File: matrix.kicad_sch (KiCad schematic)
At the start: 0 parts

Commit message: Placing Finished
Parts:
- added D1, D10, D11, D12, D13, D14, D15, D16, D17, D18, D19, D2, D20, D21, D22, D23, D24, D25, D26, D27, D28, D29, D3, D30, D31, D32, D33, D34, D35, D36, D37, D38, D39, D4, D40, D41, D42, D43, D44, D45, D46, D47, D48, D49, D5, D50, D51, D52, D53, D54, D55, D56, D57, D58, D59, D6, D60, D61, D62, D63, D64, D65, D66, D67, D68, D69, D7, D70, D71, D72, D73, D74, D8, D9: SOD-123, Diode_SMD:D_SOD-123, symbol Device:D_Small
- added MX1, MX10, MX11, MX12, MX13, MX14, MX15, MX16, MX17, MX18, MX19, MX2, MX20, MX21, MX22, MX23, MX24, MX25, MX26, MX27, MX28, MX29, MX3, MX30, MX31, MX32, MX33, MX34, MX35, MX36, MX37, MX38, MX39, MX4, MX40, MX41, MX42, MX43, MX44, MX45, MX46, MX47, MX48, MX49, MX5, MX50, MX51, MX52, MX53, MX54, MX55, MX56, MX57, MX58, MX59, MX6, MX60, MX61, MX62, MX63, MX64, MX65, MX66, MX67, MX68, MX69, MX7, MX70, MX71, MX72, MX73, MX74, MX8, MX9: MX-NoLED, marbastlib-mx:SW_MX_HS_1u, symbol MX_Alps_Hybrid:MX-NoLED
- added S73: MX_stab, marbastlib-mx:STAB_MX_2u, symbol marbastlib-mx:MX_stab
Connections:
- new net: D29.2 (A), MX29.2 (ROW)
- new net: D26.2 (A), MX26.2 (ROW)
- new net: D41.2 (A), MX41.2 (ROW)
- new net: D67.2 (A), MX67.2 (ROW)
- new net: D7.2 (A), MX7.2 (ROW)
- new net: D74.2 (A), MX74.2 (ROW)
- new net: D69.2 (A), MX69.2 (ROW)
- new net: D25.2 (A), MX25.2 (ROW)
- new net: D27.2 (A), MX27.2 (ROW)
- new net: D21.2 (A), MX21.2 (ROW)
- new net: D14.2 (A), MX14.2 (ROW)
- new net: D35.2 (A), MX35.2 (ROW)
- new net: D68.2 (A), MX68.2 (ROW)
- new net: D22.2 (A), MX22.2 (ROW)
- new net: D36.2 (A), MX36.2 (ROW)
- new net: D2.2 (A), MX2.2 (ROW)
- new net: D70.2 (A), MX70.2 (ROW)
- new net: D62.2 (A), MX62.2 (ROW)
- new net: D23.2 (A), MX23.2 (ROW)
- new net: D18.2 (A), MX18.2 (ROW)
- new net: D50.2 (A), MX50.2 (ROW)
- new net: D45.2 (A), MX45.2 (ROW)
- new net: D43.2 (A), MX43.2 (ROW)
- new net: D64.2 (A), MX64.2 (ROW)
- new net: D51.2 (A), MX51.2 (ROW)
- new net: D52.2 (A), MX52.2 (ROW)
- new net: D6.2 (A), MX6.2 (ROW)
- new net: D59.2 (A), MX59.2 (ROW)
- new net: D11.2 (A), MX11.2 (ROW)
- new net: D33.2 (A), MX33.2 (ROW)
- new net: D4.2 (A), MX4.2 (ROW)
- new net: D39.2 (A), MX39.2 (ROW)
- new net: D5.2 (A), MX5.2 (ROW)
- new net: D55.2 (A), MX55.2 (ROW)
- new net: D61.2 (A), MX61.2 (ROW)
- new net: D16.2 (A), MX16.2 (ROW)
- new net: D72.2 (A), MX72.2 (ROW)
- new net: D48.2 (A), MX48.2 (ROW)
- new net: D73.2 (A), MX73.2 (ROW)
- new net: D12.2 (A), MX12.2 (ROW)
- new net: D37.2 (A), MX37.2 (ROW)
- new net: D71.2 (A), MX71.2 (ROW)
- new net: D31.2 (A), MX31.2 (ROW)
- new net: D1.2 (A), MX1.2 (ROW)
- new net: D28.2 (A), MX28.2 (ROW)
- new net: D65.2 (A), MX65.2 (ROW)
- new net: D49.2 (A), MX49.2 (ROW)
- new net: D17.2 (A), MX17.2 (ROW)
- new net: D3.2 (A), MX3.2 (ROW)
- new net: D60.2 (A), MX60.2 (ROW)
- new net: D42.2 (A), MX42.2 (ROW)
- new net: D40.2 (A), MX40.2 (ROW)
- new net: D9.2 (A), MX9.2 (ROW)
- new net: D24.2 (A), MX24.2 (ROW)
- new net: D38.2 (A), MX38.2 (ROW)
- new net: D8.2 (A), MX8.2 (ROW)
- new net: D10.2 (A), MX10.2 (ROW)
- new net: D63.2 (A), MX63.2 (ROW)
- new net: D58.2 (A), MX58.2 (ROW)
- new net: D15.2 (A), MX15.2 (ROW)
- new net: D56.2 (A), MX56.2 (ROW)
- new net: D53.2 (A), MX53.2 (ROW)
- new net: D13.2 (A), MX13.2 (ROW)
- new net: D66.2 (A), MX66.2 (ROW)
- new net: D44.2 (A), MX44.2 (ROW)
- new net: D34.2 (A), MX34.2 (ROW)
- new net: D47.2 (A), MX47.2 (ROW)
- new net: D20.2 (A), MX20.2 (ROW)
- new net: D57.2 (A), MX57.2 (ROW)
- new net: D30.2 (A), MX30.2 (ROW)
- new net: D54.2 (A), MX54.2 (ROW)
- new net: D46.2 (A), MX46.2 (ROW)
- new net: D32.2 (A), MX32.2 (ROW)
- new net: D19.2 (A), MX19.2 (ROW)
- new net COL0: MX1.1 (COL), MX10.1 (COL), MX18.1 (COL), MX25.1 (COL), MX33.1 (COL), MX42.1 (COL), MX51.1 (COL), MX57.1 (COL), MX66.1 (COL)
- new net COL2: MX12.1 (COL), MX20.1 (COL), MX27.1 (COL), MX3.1 (COL), MX35.1 (COL), MX44.1 (COL), MX53.1 (COL), MX59.1 (COL), MX68.1 (COL)
- new net COL3: MX13.1 (COL), MX21.1 (COL), MX28.1 (COL), MX36.1 (COL), MX4.1 (COL), MX45.1 (COL), MX54.1 (COL), MX60.1 (COL), MX69.1 (COL)
- new net COL4: MX14.1 (COL), MX22.1 (COL), MX29.1 (COL), MX37.1 (COL), MX46.1 (COL), MX5.1 (COL), MX55.1 (COL), MX61.1 (COL), MX70.1 (COL)
- new net COL5: MX15.1 (COL), MX23.1 (COL), MX30.1 (COL), MX38.1 (COL), MX47.1 (COL), MX56.1 (COL), MX6.1 (COL), MX62.1 (COL), MX71.1 (COL)
- new net COL6: MX16.1 (COL), MX31.1 (COL), MX39.1 (COL), MX48.1 (COL), MX63.1 (COL), MX7.1 (COL), MX72.1 (COL)
- new net COL7: MX17.1 (COL), MX24.1 (COL), MX32.1 (COL), MX40.1 (COL), MX49.1 (COL), MX64.1 (COL), MX73.1 (COL), MX8.1 (COL)
- new net COL8: MX41.1 (COL), MX50.1 (COL), MX65.1 (COL), MX74.1 (COL), MX9.1 (COL)
- new net ROW0: D1.1 (K), D2.1 (K), D3.1 (K), D4.1 (K), D5.1 (K), D6.1 (K), D7.1 (K), D8.1 (K), D9.1 (K)
- new net ROW1: D10.1 (K), D11.1 (K), D12.1 (K), D13.1 (K), D14.1 (K), D15.1 (K), D16.1 (K), D17.1 (K)
- new net ROW2: D18.1 (K), D19.1 (K), D20.1 (K), D21.1 (K), D22.1 (K), D23.1 (K), D24.1 (K)
- new net ROW3: D25.1 (K), D26.1 (K), D27.1 (K), D28.1 (K), D29.1 (K), D30.1 (K), D31.1 (K), D32.1 (K)
- new net ROW4: D33.1 (K), D34.1 (K), D35.1 (K), D36.1 (K), D37.1 (K), D38.1 (K), D39.1 (K), D40.1 (K), D41.1 (K)
- new net ROW5: D42.1 (K), D43.1 (K), D44.1 (K), D45.1 (K), D46.1 (K), D47.1 (K), D48.1 (K), D49.1 (K), D50.1 (K)
- new net ROW6: D51.1 (K), D52.1 (K), D53.1 (K), D54.1 (K), D55.1 (K), D56.1 (K)
- new net ROW7: D57.1 (K), D58.1 (K), D59.1 (K), D60.1 (K), D61.1 (K), D62.1 (K), D63.1 (K), D64.1 (K), D65.1 (K)
- new net ROW8: D66.1 (K), D67.1 (K), D68.1 (K), D69.1 (K), D70.1 (K), D71.1 (K), D72.1 (K), D73.1 (K), D74.1 (K)
- new net cOL1: MX11.1 (COL), MX19.1 (COL), MX2.1 (COL), MX26.1 (COL), MX34.1 (COL), MX43.1 (COL), MX52.1 (COL), MX58.1 (COL), MX67.1 (COL)
- no-connect marks 0 -> 74
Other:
- note added: "Row 0"
- note added: "Row 1"
- note added: "Row 2"
- note added: "Row 3"
- note added: "Row 4"
- note added: "Row 5"
- note added: "Row 6"
- note added: "Row 7"
- note added: "Row 8"

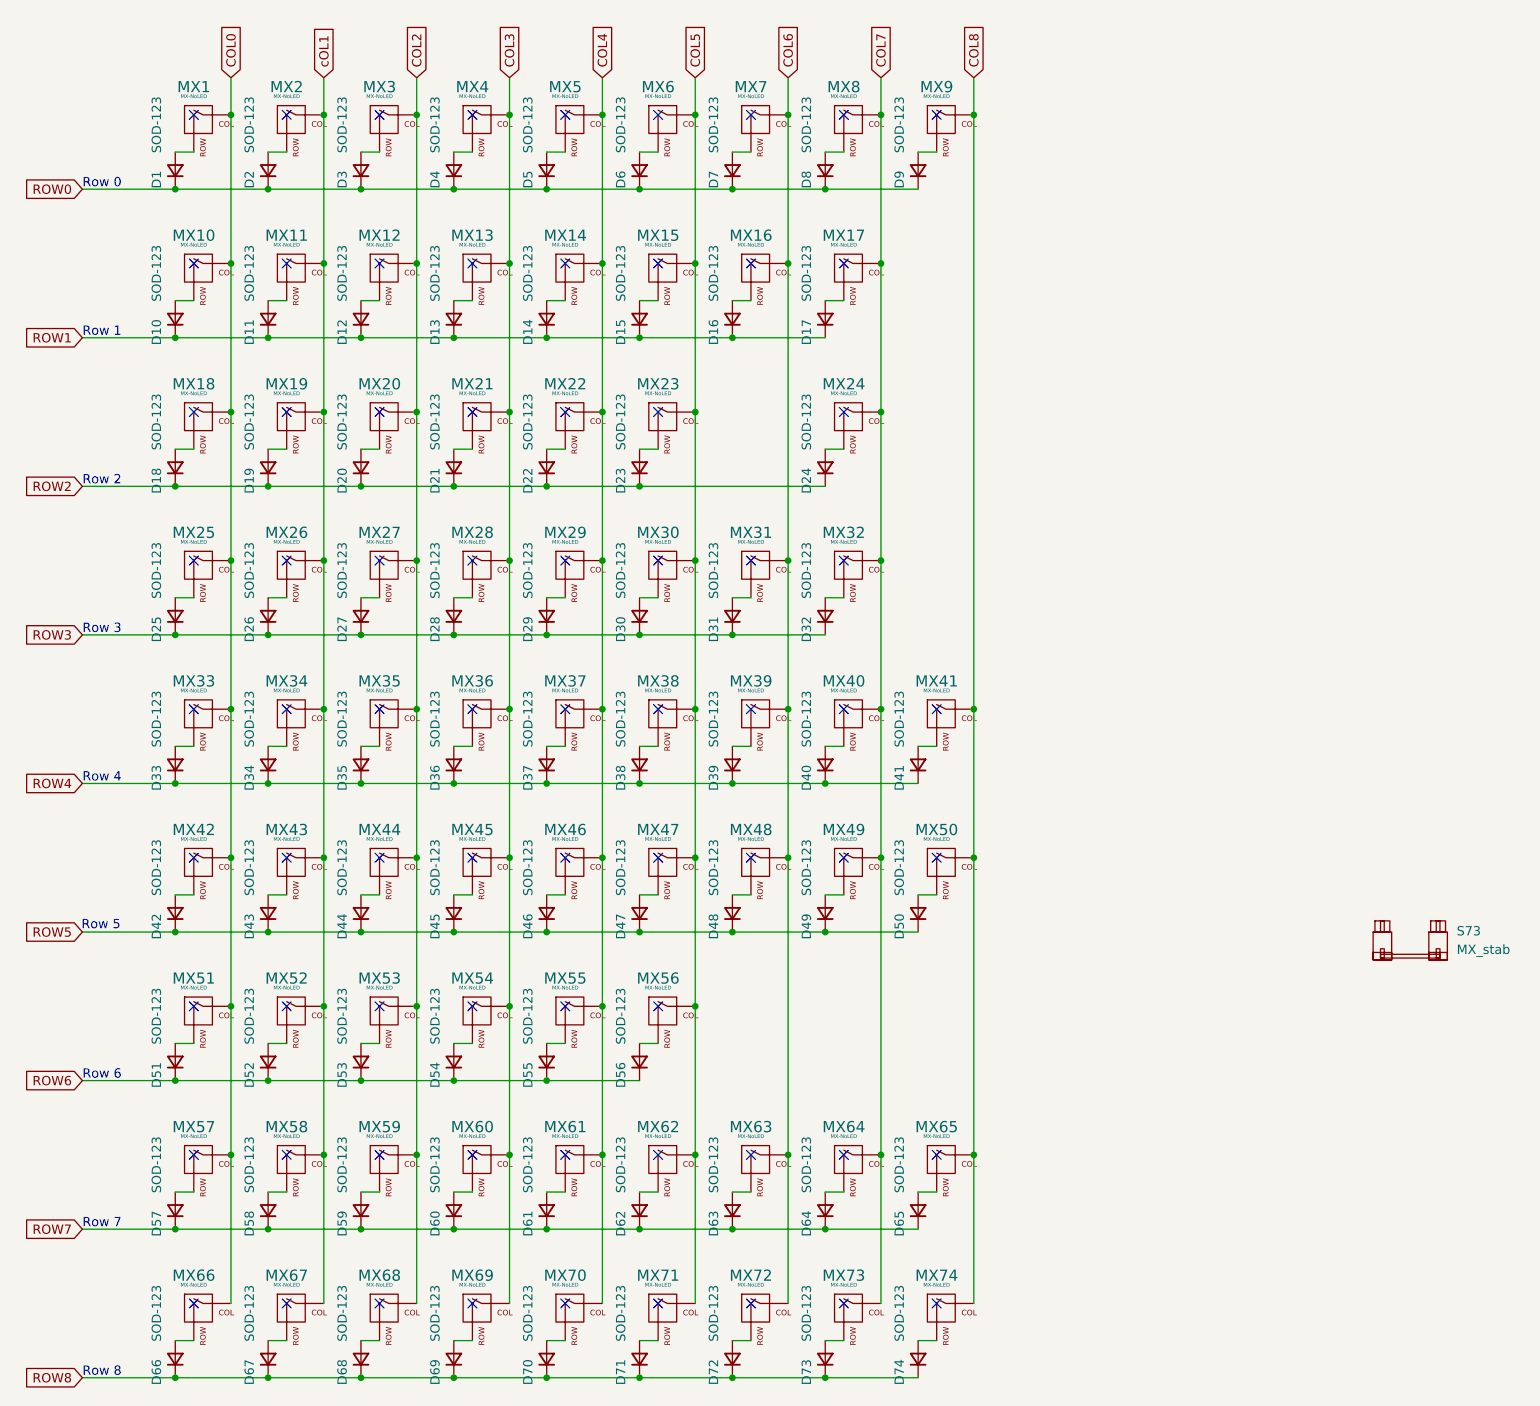
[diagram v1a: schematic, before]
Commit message: Matrix Traces in
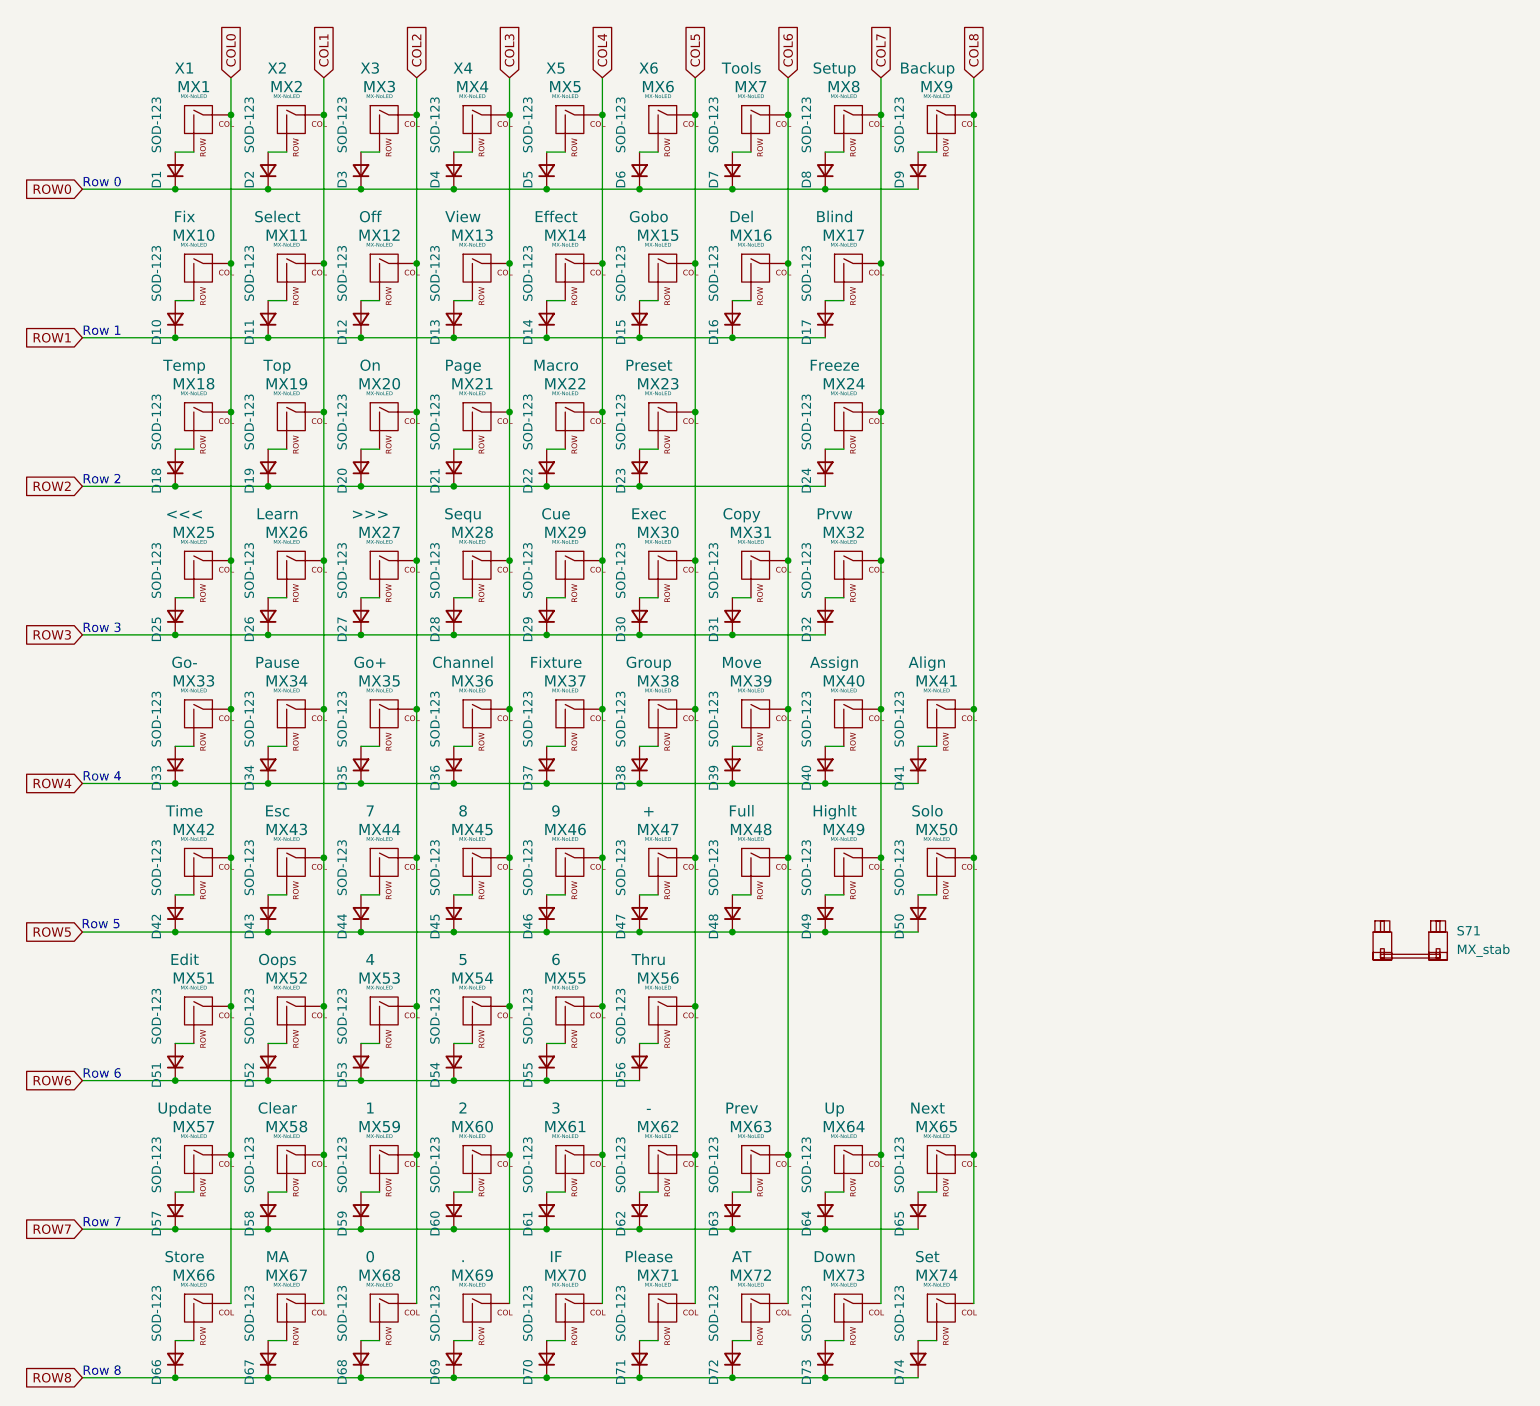
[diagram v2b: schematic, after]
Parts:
- MX1: footprint marbastlib-mx:SW_MX_HS_1u -> MX_Only:MXOnly-1U-Hotswap-Antishear-Dvdcd-Mod; Label (none) -> X1
- MX10: footprint marbastlib-mx:SW_MX_HS_1u -> MX_Only:MXOnly-1U-Hotswap-Antishear-Dvdcd-Mod; Label (none) -> Fix
- MX11: footprint marbastlib-mx:SW_MX_HS_1u -> MX_Only:MXOnly-1U-Hotswap-Antishear-Dvdcd-Mod; Label (none) -> Select
- MX12: footprint marbastlib-mx:SW_MX_HS_1u -> MX_Only:MXOnly-1U-Hotswap-Antishear-Dvdcd-Mod; Label (none) -> Off
- MX13: footprint marbastlib-mx:SW_MX_HS_1u -> MX_Only:MXOnly-1U-Hotswap-Antishear-Dvdcd-Mod; Label (none) -> View
- MX14: footprint marbastlib-mx:SW_MX_HS_1u -> MX_Only:MXOnly-1U-Hotswap-Antishear-Dvdcd-Mod; Label (none) -> Effect
- MX15: footprint marbastlib-mx:SW_MX_HS_1u -> MX_Only:MXOnly-1U-Hotswap-Antishear-Dvdcd-Mod; Label (none) -> Gobo
- MX16: footprint marbastlib-mx:SW_MX_HS_1u -> MX_Only:MXOnly-1U-Hotswap-Antishear-Dvdcd-Mod; Label (none) -> Del
- MX17: footprint marbastlib-mx:SW_MX_HS_1u -> MX_Only:MXOnly-1U-Hotswap-Antishear-Dvdcd-Mod; Label (none) -> Blind
- MX18: footprint marbastlib-mx:SW_MX_HS_1u -> MX_Only:MXOnly-1U-Hotswap-Antishear-Dvdcd-Mod; Label (none) -> Temp
- MX19: footprint marbastlib-mx:SW_MX_HS_1u -> MX_Only:MXOnly-1U-Hotswap-Antishear-Dvdcd-Mod; Label (none) -> Top
- MX2: footprint marbastlib-mx:SW_MX_HS_1u -> MX_Only:MXOnly-1U-Hotswap-Antishear-Dvdcd-Mod; Label (none) -> X2
- MX20: footprint marbastlib-mx:SW_MX_HS_1u -> MX_Only:MXOnly-1U-Hotswap-Antishear-Dvdcd-Mod; Label (none) -> On
- MX21: footprint marbastlib-mx:SW_MX_HS_1u -> MX_Only:MXOnly-1U-Hotswap-Antishear-Dvdcd-Mod; Label (none) -> Page
- MX22: footprint marbastlib-mx:SW_MX_HS_1u -> MX_Only:MXOnly-1U-Hotswap-Antishear-Dvdcd-Mod; Label (none) -> Macro
- MX23: footprint marbastlib-mx:SW_MX_HS_1u -> MX_Only:MXOnly-1U-Hotswap-Antishear-Dvdcd-Mod; Label (none) -> Preset
- MX24: footprint marbastlib-mx:SW_MX_HS_1u -> MX_Only:MXOnly-1U-Hotswap-Antishear-Dvdcd-Mod; Label (none) -> Freeze
- MX25: footprint marbastlib-mx:SW_MX_HS_1u -> MX_Only:MXOnly-1U-Hotswap-Antishear-Dvdcd-Mod; Label (none) -> <<<
- MX26: footprint marbastlib-mx:SW_MX_HS_1u -> MX_Only:MXOnly-1U-Hotswap-Antishear-Dvdcd-Mod; Label (none) -> Learn
- MX27: footprint marbastlib-mx:SW_MX_HS_1u -> MX_Only:MXOnly-1U-Hotswap-Antishear-Dvdcd-Mod; Label (none) -> >>>
- MX28: footprint marbastlib-mx:SW_MX_HS_1u -> MX_Only:MXOnly-1U-Hotswap-Antishear-Dvdcd-Mod; Label (none) -> Sequ
- MX29: footprint marbastlib-mx:SW_MX_HS_1u -> MX_Only:MXOnly-1U-Hotswap-Antishear-Dvdcd-Mod; Label (none) -> Cue
- MX3: footprint marbastlib-mx:SW_MX_HS_1u -> MX_Only:MXOnly-1U-Hotswap-Antishear-Dvdcd-Mod; Label (none) -> X3
- MX30: footprint marbastlib-mx:SW_MX_HS_1u -> MX_Only:MXOnly-1U-Hotswap-Antishear-Dvdcd-Mod; Label (none) -> Exec
- MX31: footprint marbastlib-mx:SW_MX_HS_1u -> MX_Only:MXOnly-1U-Hotswap-Antishear-Dvdcd-Mod; Label (none) -> Copy
- MX32: footprint marbastlib-mx:SW_MX_HS_1u -> MX_Only:MXOnly-1U-Hotswap-Antishear-Dvdcd-Mod; Label (none) -> Prvw
- MX33: footprint marbastlib-mx:SW_MX_HS_1u -> MX_Only:MXOnly-1U-Hotswap-Antishear-Dvdcd-Mod; Label (none) -> Go-
- MX34: footprint marbastlib-mx:SW_MX_HS_1u -> MX_Only:MXOnly-1U-Hotswap-Antishear-Dvdcd-Mod; Label (none) -> Pause
- MX35: footprint marbastlib-mx:SW_MX_HS_1u -> MX_Only:MXOnly-1U-Hotswap-Antishear-Dvdcd-Mod; Label (none) -> Go+
- MX36: footprint marbastlib-mx:SW_MX_HS_1u -> MX_Only:MXOnly-1U-Hotswap-Antishear-Dvdcd-Mod; Label (none) -> Channel
- MX37: footprint marbastlib-mx:SW_MX_HS_1u -> MX_Only:MXOnly-1U-Hotswap-Antishear-Dvdcd-Mod; Label (none) -> Fixture
- MX38: footprint marbastlib-mx:SW_MX_HS_1u -> MX_Only:MXOnly-1U-Hotswap-Antishear-Dvdcd-Mod; Label (none) -> Group
- MX39: footprint marbastlib-mx:SW_MX_HS_1u -> MX_Only:MXOnly-1U-Hotswap-Antishear-Dvdcd-Mod; Label (none) -> Move
- MX4: footprint marbastlib-mx:SW_MX_HS_1u -> MX_Only:MXOnly-1U-Hotswap-Antishear-Dvdcd-Mod; Label (none) -> X4
- MX40: footprint marbastlib-mx:SW_MX_HS_1u -> MX_Only:MXOnly-1U-Hotswap-Antishear-Dvdcd-Mod; Label (none) -> Assign
- MX41: footprint marbastlib-mx:SW_MX_HS_1u -> MX_Only:MXOnly-1U-Hotswap-Antishear-Dvdcd-Mod; Label (none) -> Align
- MX42: footprint marbastlib-mx:SW_MX_HS_1u -> MX_Only:MXOnly-1U-Hotswap-Antishear-Dvdcd-Mod; Label (none) -> Time
- MX43: footprint marbastlib-mx:SW_MX_HS_1u -> MX_Only:MXOnly-1U-Hotswap-Antishear-Dvdcd-Mod; Label (none) -> Esc
- MX44: footprint marbastlib-mx:SW_MX_HS_1u -> MX_Only:MXOnly-1U-Hotswap-Antishear-Dvdcd-Mod; Label (none) -> 7
- MX45: footprint marbastlib-mx:SW_MX_HS_1u -> MX_Only:MXOnly-1U-Hotswap-Antishear-Dvdcd-Mod; Label (none) -> 8
- MX46: footprint marbastlib-mx:SW_MX_HS_1u -> MX_Only:MXOnly-1U-Hotswap-Antishear-Dvdcd-Mod; Label (none) -> 9
- MX47: footprint marbastlib-mx:SW_MX_HS_1u -> MX_Only:MXOnly-1U-Hotswap-Antishear-Dvdcd-Mod; Label (none) -> +
- MX48: footprint marbastlib-mx:SW_MX_HS_1u -> MX_Only:MXOnly-1U-Hotswap-Antishear-Dvdcd-Mod; Label (none) -> Full
- MX49: footprint marbastlib-mx:SW_MX_HS_1u -> MX_Only:MXOnly-1U-Hotswap-Antishear-Dvdcd-Mod; Label (none) -> Highlt
- MX5: footprint marbastlib-mx:SW_MX_HS_1u -> MX_Only:MXOnly-1U-Hotswap-Antishear-Dvdcd-Mod; Label (none) -> X5
- MX50: footprint marbastlib-mx:SW_MX_HS_1u -> MX_Only:MXOnly-1U-Hotswap-Antishear-Dvdcd-Mod; Label (none) -> Solo
- MX51: footprint marbastlib-mx:SW_MX_HS_1u -> MX_Only:MXOnly-1U-Hotswap-Antishear-Dvdcd-Mod; Label (none) -> Edit
- MX52: footprint marbastlib-mx:SW_MX_HS_1u -> MX_Only:MXOnly-1U-Hotswap-Antishear-Dvdcd-Mod; Label (none) -> Oops
- MX53: footprint marbastlib-mx:SW_MX_HS_1u -> MX_Only:MXOnly-1U-Hotswap-Antishear-Dvdcd-Mod; Label (none) -> 4
- MX54: footprint marbastlib-mx:SW_MX_HS_1u -> MX_Only:MXOnly-1U-Hotswap-Antishear-Dvdcd-Mod; Label (none) -> 5
- MX55: footprint marbastlib-mx:SW_MX_HS_1u -> MX_Only:MXOnly-1U-Hotswap-Antishear-Dvdcd-Mod; Label (none) -> 6
- MX56: footprint marbastlib-mx:SW_MX_HS_1u -> MX_Only:MXOnly-1U-Hotswap-Antishear-Dvdcd-Mod; Label (none) -> Thru
- MX57: footprint marbastlib-mx:SW_MX_HS_1u -> MX_Only:MXOnly-1U-Hotswap-Antishear-Dvdcd-Mod; Label (none) -> Update
- MX58: footprint marbastlib-mx:SW_MX_HS_1u -> MX_Only:MXOnly-1U-Hotswap-Antishear-Dvdcd-Mod; Label (none) -> Clear
- MX59: footprint marbastlib-mx:SW_MX_HS_1u -> MX_Only:MXOnly-1U-Hotswap-Antishear-Dvdcd-Mod; Label (none) -> 1
- MX6: footprint marbastlib-mx:SW_MX_HS_1u -> MX_Only:MXOnly-1U-Hotswap-Antishear-Dvdcd-Mod; Label (none) -> X6
- MX60: footprint marbastlib-mx:SW_MX_HS_1u -> MX_Only:MXOnly-1U-Hotswap-Antishear-Dvdcd-Mod; Label (none) -> 2
- MX61: footprint marbastlib-mx:SW_MX_HS_1u -> MX_Only:MXOnly-1U-Hotswap-Antishear-Dvdcd-Mod; Label (none) -> 3
- MX62: footprint marbastlib-mx:SW_MX_HS_1u -> MX_Only:MXOnly-1U-Hotswap-Antishear-Dvdcd-Mod; Label (none) -> -
- MX63: footprint marbastlib-mx:SW_MX_HS_1u -> MX_Only:MXOnly-1U-Hotswap-Antishear-Dvdcd-Mod; Label (none) -> Prev
- MX64: footprint marbastlib-mx:SW_MX_HS_1u -> MX_Only:MXOnly-1U-Hotswap-Antishear-Dvdcd-Mod; Label (none) -> Up
- MX65: footprint marbastlib-mx:SW_MX_HS_1u -> MX_Only:MXOnly-1U-Hotswap-Antishear-Dvdcd-Mod; Label (none) -> Next
- MX66: footprint marbastlib-mx:SW_MX_HS_1u -> MX_Only:MXOnly-1U-Hotswap-Antishear-Dvdcd-Mod; Label (none) -> Store
- MX67: footprint marbastlib-mx:SW_MX_HS_1u -> MX_Only:MXOnly-1U-Hotswap-Antishear-Dvdcd-Mod; Label (none) -> MA
- MX68: footprint marbastlib-mx:SW_MX_HS_1u -> MX_Only:MXOnly-1U-Hotswap-Antishear-Dvdcd-Mod; Label (none) -> 0
- MX69: footprint marbastlib-mx:SW_MX_HS_1u -> MX_Only:MXOnly-1U-Hotswap-Antishear-Dvdcd-Mod; Label (none) -> .
- MX7: footprint marbastlib-mx:SW_MX_HS_1u -> MX_Only:MXOnly-1U-Hotswap-Antishear-Dvdcd-Mod; Label (none) -> Tools
- MX70: footprint marbastlib-mx:SW_MX_HS_1u -> MX_Only:MXOnly-1U-Hotswap-Antishear-Dvdcd-Mod; Label (none) -> IF
- MX71: footprint marbastlib-mx:SW_MX_HS_1u -> MX_Only:MXOnly-1U-Hotswap-Antishear-Dvdcd-Mod; Label (none) -> Please
- MX72: footprint marbastlib-mx:SW_MX_HS_1u -> MX_Only:MXOnly-1U-Hotswap-Antishear-Dvdcd-Mod; Label (none) -> AT
- MX73: footprint marbastlib-mx:SW_MX_HS_1u -> MX_Only:MXOnly-1U-Hotswap-Antishear-Dvdcd-Mod; Label (none) -> Down
- MX74: footprint marbastlib-mx:SW_MX_HS_1u -> MX_Only:MXOnly-1U-Hotswap-Antishear-Dvdcd-Mod; Label (none) -> Set
- MX8: footprint marbastlib-mx:SW_MX_HS_1u -> MX_Only:MXOnly-1U-Hotswap-Antishear-Dvdcd-Mod; Label (none) -> Setup
- MX9: footprint marbastlib-mx:SW_MX_HS_1u -> MX_Only:MXOnly-1U-Hotswap-Antishear-Dvdcd-Mod; Label (none) -> Backup
- renumbered S73 to S71
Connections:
- net cOL1 renamed COL1
- no-connect marks 74 -> 0
